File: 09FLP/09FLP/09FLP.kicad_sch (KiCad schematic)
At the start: 51 parts, among them J1 Floppy, J2 Floppy, J3 Floppy_50p, Q1 BS170, Q2 BS170, U1 74HC245, U13 74HC273, U2 GAL16V8, U3 WD2793, U4 74HC240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

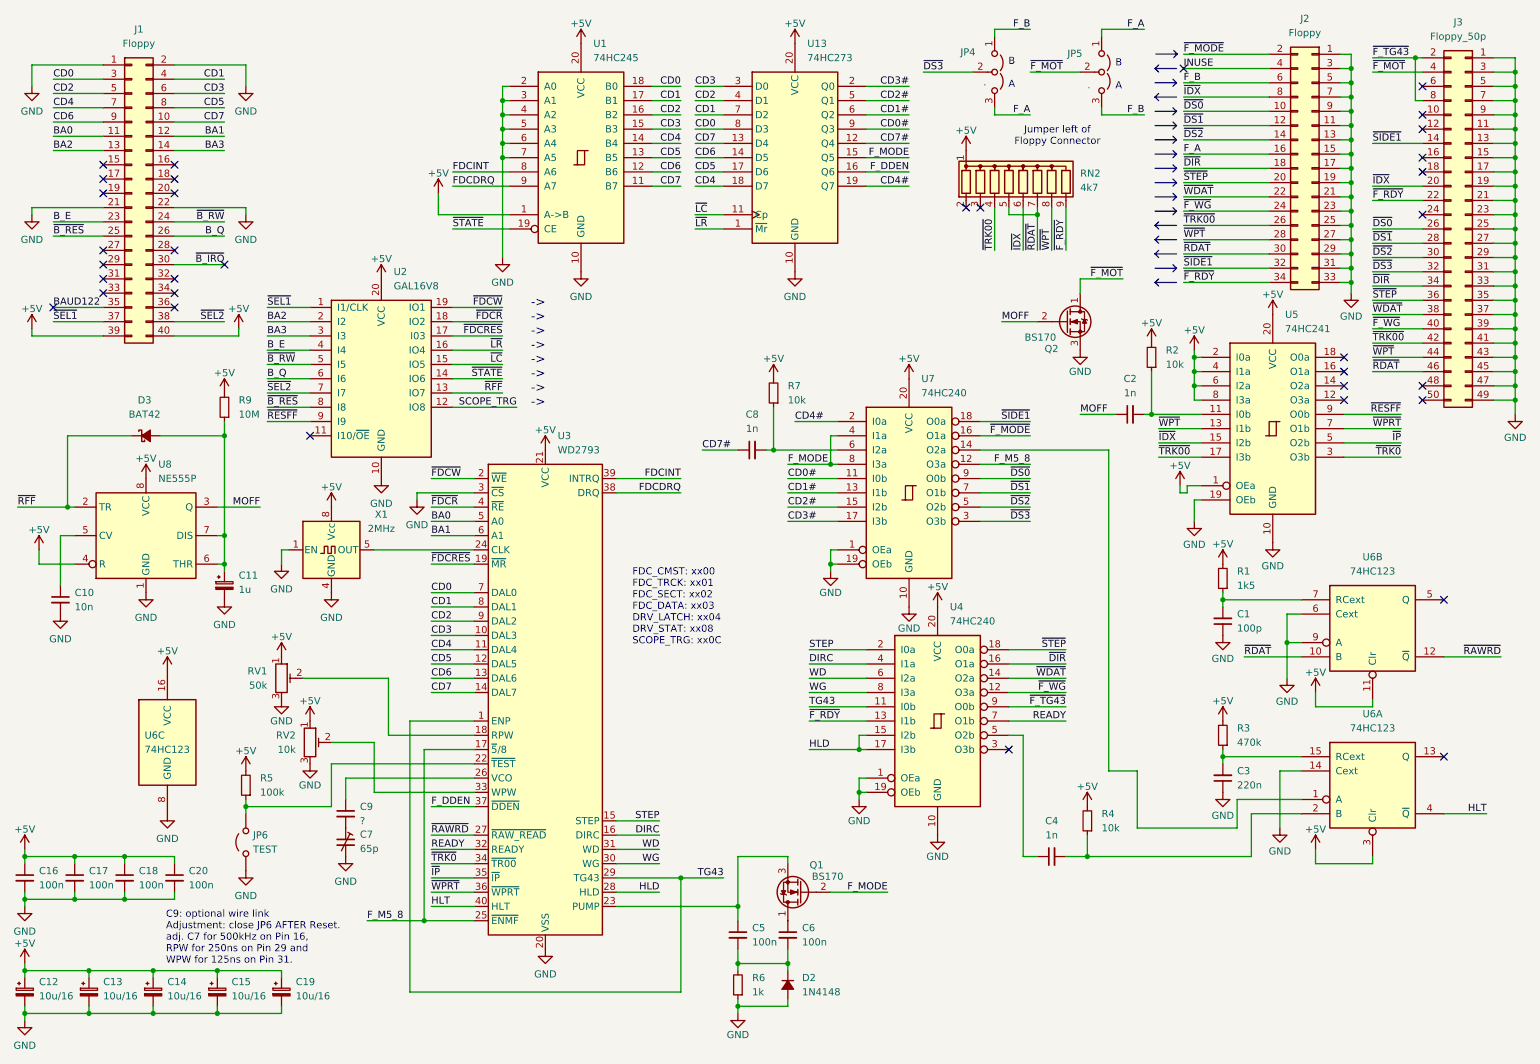
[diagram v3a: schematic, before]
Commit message: new CPU09US4 Board added
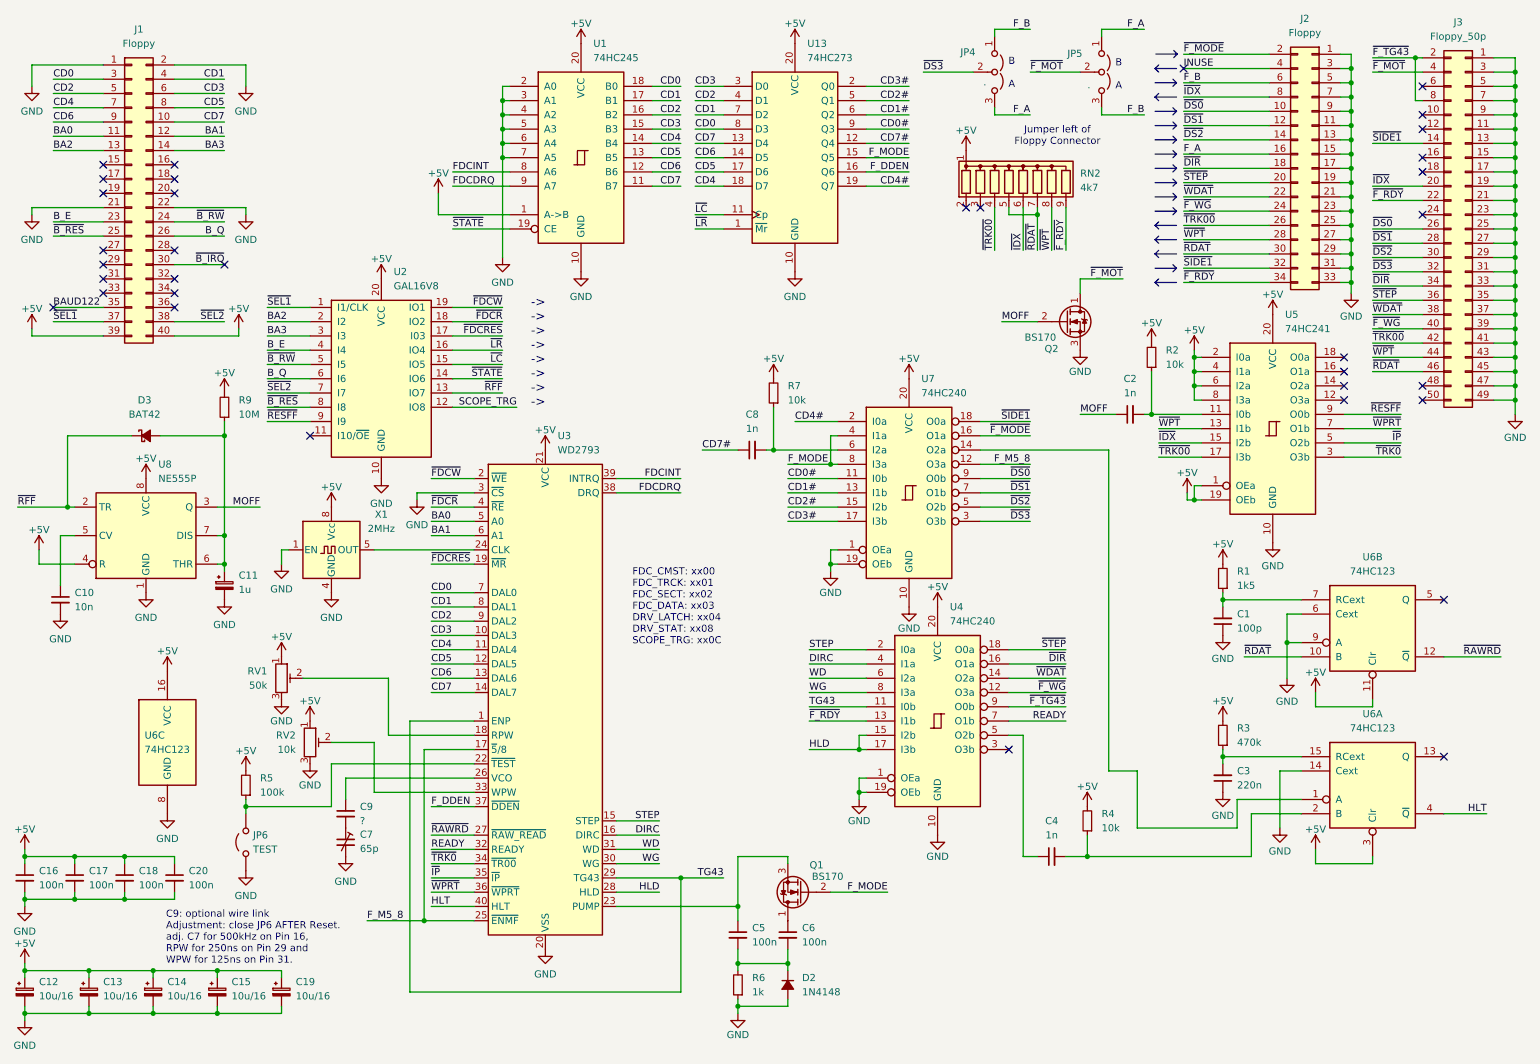
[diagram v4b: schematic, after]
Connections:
- net +5V: now also U5.19 (OEb)
- net GND: no longer U5.19 (OEb)
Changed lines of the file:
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@@
 (kicad_sch
-	(version 20231120)
+	(version 20250114)
 	(generator "eeschema")
-	(generator_version "8.0")
+	(generator_version "9.0")
 	(paper "A4")
 	(title_block
 		(title "09FLP")
 		(date "2025-02-01")
-		(rev "v1.11")
+		(rev "v1.12")
 		(company "100% Offner")
 		(comment 1 "redraw from kees1948 FLEX and UniFLEX System")
 		(comment 2 "v1.1: ch. C3, ch. all 74LS Types to HC")
 		(comment 3 "v1.11: Direction of J2 Pin 2 ch., Instructions updated")
+		(comment 4 "v1.12: U5-19 to +5V")
+	)
+	(text "Jumper left of\nFloppy Connector"
+		(exclude_from_sim no)
+		(at 200.406 34.29 0)
+		(effects
+			(font
+				(size 1.27 1.27)
+			)
+		)
+	)
+	(text "->\n->\n->\n->\n->\n->\n->\n->\n"
+		(exclude_from_sim no)
+		(at 107.95 72.898 0)
+		(effects
+			(font
+				(size 1.5748 1.5748)
+			)
+		)
+	)
+	(text "B\n\nA\n"
+		(exclude_from_sim no)
+		(at 211.328 23.368 0)
+		(effects
+			(font
+				(size 1.27 1.27)
+			)
+		)
+	)
+	(text "C9: optional wire link\nAdjustment: close JP6 AFTER Reset.\nadj. C7 for 500kHz on Pin 16,\nRPW for 250ns on Pin 29 and\nWPW for 125ns on Pin 31."
+		(exclude_from_sim no)
+		(at 41.656 177.038 0)
+		(effects
+			(font
+				(size 1.27 1.27)
+			)
+			(justify left)
+		)
+	)
+	(text "FDC_CMST: xx00\nFDC_TRCK: xx01\nFDC_SECT: xx02\nFDC_DATA: xx03\nDRV_LATCH: xx04\nDRV_STAT: xx08\nSCOPE_TRG: xx0C"
+		(exclude_from_sim no)
+		(at 124.714 118.11 0)
+		(effects
+			(font
+				(size 1.27 1.27)
+			)
+			(justify left)
+		)
+	)
+	(text "B\n\nA\n"
+		(exclude_from_sim no)
+		(at 192.278 23.114 0)
+		(effects
+			(font
+				(size 1.27 1.27)
+			)
+		)
 	)
 	(junction
@@
 	)
 	(junction
+		(at 224.79 99.06)
+		(diameter 0)
+		(color 0 0 0 0)
+	)
+	(junction
 		(at 281.94 38.1)
 		(diameter 0)
@@
 	(wire
 		(pts
-			(xy 222.25 97.79) (xy 222.25 96.52)
+			(xy 223.52 99.06) (xy 223.52 97.79)
 		)
 		(stroke
@@
 	(wire
 		(pts
-			(xy 226.06 96.52) (xy 223.52 96.52)
-		)
-		(stroke
-			(width 0)
-			(type default)
-		)
-	)
-	(wire
-		(pts
 			(xy 252.73 40.005) (xy 252.73 42.545)
 		)
@@
 		)
 	)
-	(wire
-		(pts
-			(xy 223.52 96.52) (xy 223.52 97.79)
-		)
-		(stroke
-			(width 0)
-			(type default)
-		)
-	)
 	(polyline
 		(pts
@@
 	(wire
 		(pts
-			(xy 214.63 157.48) (xy 214.63 147.32)
+			(xy 224.79 99.06) (xy 224.79 96.52)
 		)
 		(stroke
@@
 	(wire
 		(pts
-			(xy 224.79 99.06) (xy 226.06 99.06)
+			(xy 214.63 157.48) (xy 214.63 147.32)
 		)
 		(stroke
@@
 	(wire
 		(pts
+			(xy 224.79 96.52) (xy 226.06 96.52)
+		)
+		(stroke
+			(width 0)
+			(type default)
+		)
+	)
+	(wire
+		(pts
 			(xy 92.71 80.01) (xy 101.6 80.01)
 		)
@@
 	(wire
 		(pts
-			(xy 224.79 99.06) (xy 224.79 102.87)
-		)
-		(stroke
-			(width 0)
-			(type default)
-		)
-	)
-	(wire
-		(pts
 			(xy 209.55 147.32) (xy 214.63 147.32)
 		)
@@
 	(wire
 		(pts
-			(xy 223.52 97.79) (xy 222.25 97.79)
+			(xy 224.79 99.06) (xy 223.52 99.06)
 		)
 		(stroke
@@
 	(wire
 		(pts
+			(xy 226.06 99.06) (xy 224.79 99.06)
+		)
+		(stroke
+			(width 0)
+			(type default)
+		)
+	)
+	(wire
+		(pts
 			(xy 54.61 68.58) (xy 54.61 69.85)
 		)
@@
 		)
 	)
-	(text "Jumper left of\nFloppy Connector"
-		(exclude_from_sim no)
-		(at 200.406 34.29 0)
-		(effects
-			(font
-				(size 1.27 1.27)
-			)
-		)
-	)
-	(text "->\n->\n->\n->\n->\n->\n->\n->\n"
-		(exclude_from_sim no)
-		(at 107.95 72.898 0)
-		(effects
-			(font
-				(size 1.5748 1.5748)
-			)
-		)
-	)
-	(text "B\n\nA\n"
-		(exclude_from_sim no)
-		(at 211.328 23.368 0)
-		(effects
-			(font
-				(size 1.27 1.27)
-			)
-		)
-	)
-	(text "C9: optional wire link\nAdjustment: close JP6 AFTER Reset.\nadj. C7 for 500kHz on Pin 16,\nRPW for 250ns on Pin 29 and\nWPW for 125ns on Pin 31."
-		(exclude_from_sim no)
-		(at 41.656 177.038 0)
-		(effects
-			(font
-				(size 1.27 1.27)
-			)
-			(justify left)
-		)
-	)
-	(text "FDC_CMST: xx00\nFDC_TRCK: xx01\nFDC_SECT: xx02\nFDC_DATA: xx03\nDRV_LATCH: xx04\nDRV_STAT: xx08\nSCOPE_TRG: xx0C"
-		(exclude_from_sim no)
-		(at 124.714 118.11 0)
-		(effects
-			(font
-				(size 1.27 1.27)
-			)
-			(justify left)
-		)
-	)
-	(text "B\n\nA\n"
-		(exclude_from_sim no)
-		(at 192.278 23.114 0)
-		(effects
-			(font
-				(size 1.27 1.27)
-			)
-		)
-	)
 	(label "WD"
 		(at 129.54 161.29 180)
@@
 	(symbol
 		(lib_id "power:GND")
-		(at 224.79 102.87 0)
-		(unit 1)
-		(exclude_from_sim no)
-		(in_bom yes)
-		(on_board yes)
-		(dnp no)
-		(fields_autoplaced yes)
-		(property "Reference" "#PWR056"
-			(at 224.79 109.22 0)
-			(effects
-				(font
-					(size 1.27 1.27)
-				)
-				(hide yes)
-			)
-		)
-		(property "Value" "GND"
-			(at 224.79 107.0031 0)
-			(effects
-				(font
-					(size 1.27 1.27)
-				)
-			)
-		)
-		(property "Footprint" ""
-			(at 224.79 102.87 0)
-			(effects
-				(font
-					(size 1.27 1.27)
-				)
-				(hide yes)
-			)
-		)
-		(property "Datasheet" ""
-			(at 224.79 102.87 0)
-			(effects
-				(font
-					(size 1.27 1.27)
-				)
-				(hide yes)
-			)
-		)
-		(property "Description" ""
-			(at 224.79 102.87 0)
-			(effects
-				(font
-					(size 1.27 1.27)
-				)
-				(hide yes)
-			)
-		)
-		(pin "1"
-		)
-		(instances
-			(project "09FLP"
-				(path "/f7470e71-a162-4277-ac91-f83c18bb0cc8"
-					(reference "#PWR056")
-					(unit 1)
-				)
-			)
-		)
-	)
-	(symbol
-		(lib_id "power:GND")
 		(at 55.88 48.26 0)
 		(unit 1)
@@
 	(symbol
 		(lib_id "power:+5V")
-		(at 222.25 96.52 0)
+		(at 223.52 97.79 0)
 		(mirror y)
 		(unit 1)
@@
 		(fields_autoplaced yes)
 		(property "Reference" "#PWR057"
-			(at 222.25 100.33 0)
+			(at 223.52 101.6 0)
 			(effects
 				(font
@@
 		)
 		(property "Value" "+5V"
-			(at 222.25 92.9442 0)
+			(at 223.52 94.2142 0)
 			(effects
 				(font
@@
 		)
 		(property "Footprint" ""
-			(at 222.25 96.52 0)
+			(at 223.52 97.79 0)
 			(effects
 				(font
@@
 		)
 		(property "Datasheet" ""
-			(at 222.25 96.52 0)
+			(at 223.52 97.79 0)
 			(effects
 				(font
@@
 		)
 		(property "Description" ""
-			(at 222.25 96.52 0)
+			(at 223.52 97.79 0)
 			(effects
 				(font
@@
 		)
 	)
+	(embedded_fonts no)
 )
